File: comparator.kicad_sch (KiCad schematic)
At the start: 8 parts

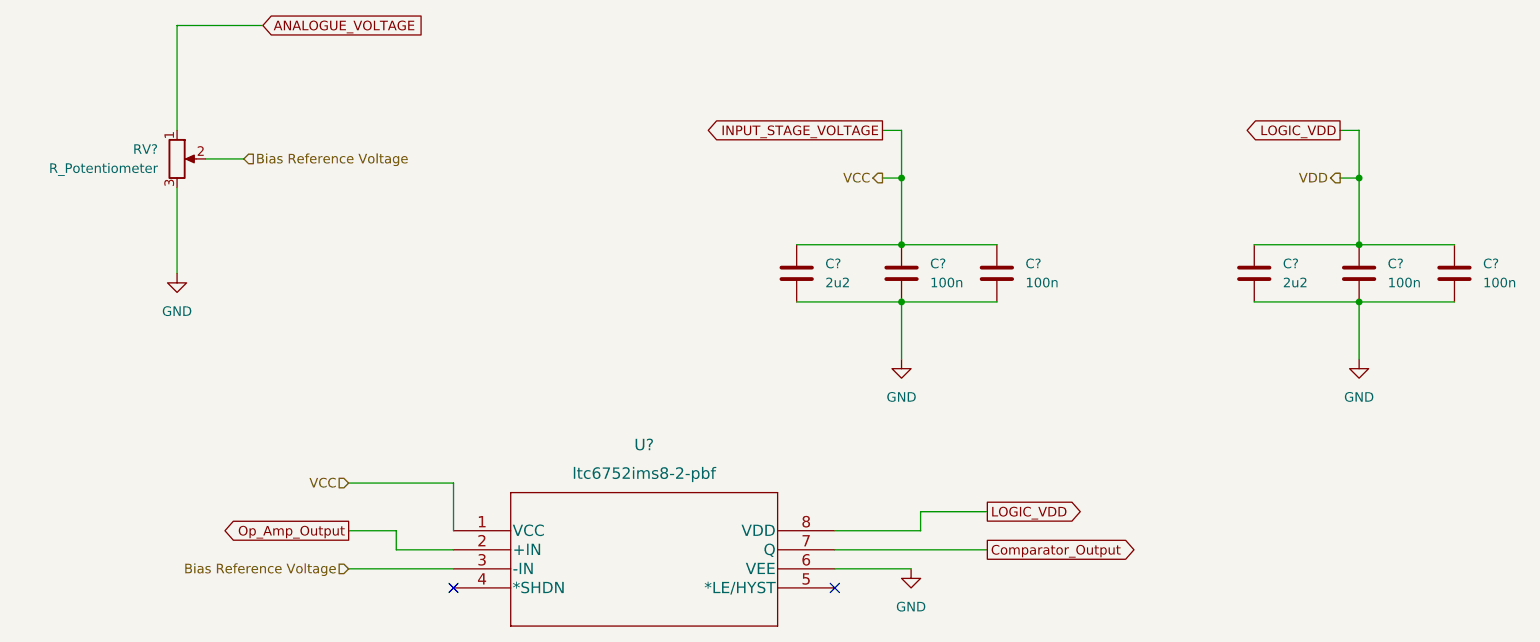
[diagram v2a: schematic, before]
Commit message: improve labels on comparator
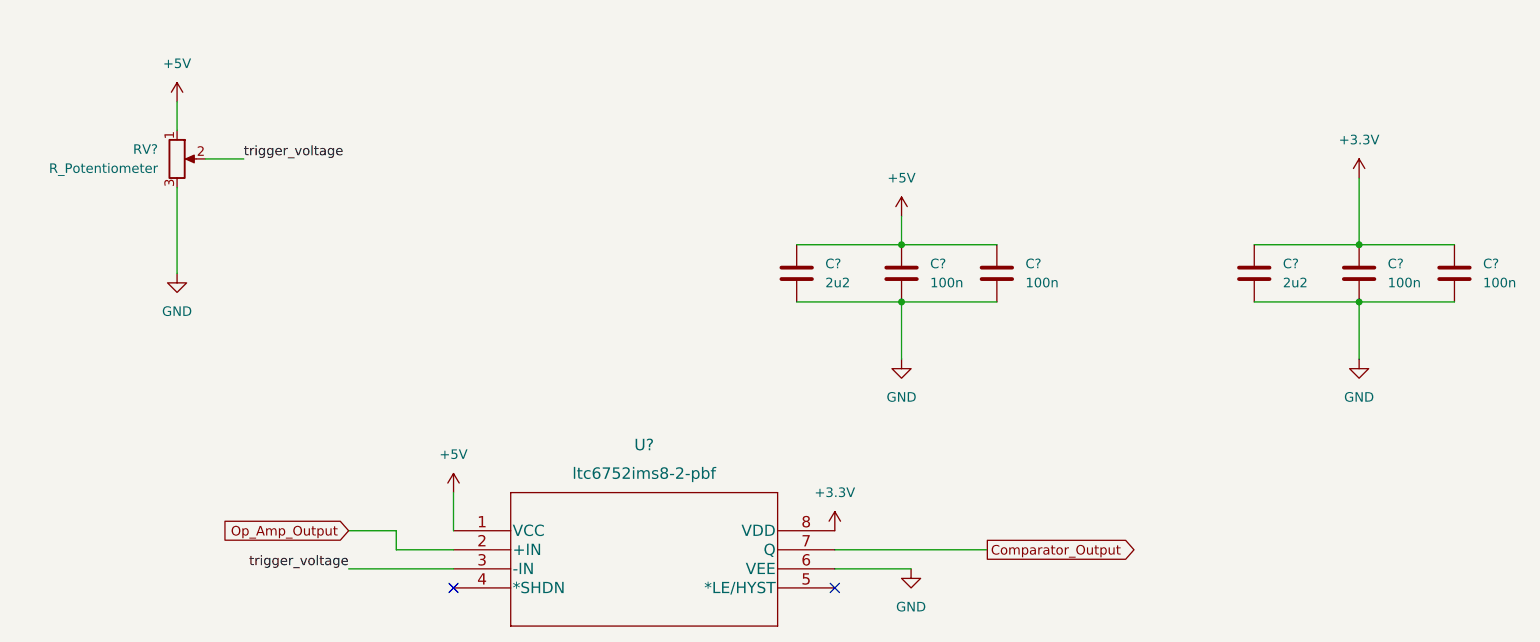
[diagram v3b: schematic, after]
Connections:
- net INPUT_STAGE_VOLTAGE is gone; now on net +5V: C?.1, C?.1, C?.1, U?.1 (VCC)
- net ANALOGUE_VOLTAGE renamed +5V
- net Bias Reference Voltage renamed trigger_voltage
- net LOGIC_VDD renamed +3.3V
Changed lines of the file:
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@@
   (junction (at 172.72 53.34) (diameter 0) (color 0 0 0 0)
   )
-  (junction (at 172.72 44.45) (diameter 0) (color 0 0 0 0)
-  )
   (junction (at 233.68 53.34) (diameter 0) (color 0 0 0 0)
   )
@@
   )
   (junction (at 172.72 60.96) (diameter 0) (color 0 0 0 0)
-  )
-  (junction (at 233.68 44.45) (diameter 0) (color 0 0 0 0)
   )
   (no_connect (at 113.03 99.06))
   (no_connect (at 163.83 99.06))
+  (wire (pts (xy 172.72 49.53) (xy 172.72 53.34))
+    (stroke (width 0) (type default) (color 0 0 0 0))
+  )
   (wire (pts (xy 233.68 60.96) (xy 246.38 60.96))
     (stroke (width 0) (type default) (color 0 0 0 0))
   )
-  (wire (pts (xy 172.72 44.45) (xy 172.72 53.34))
-    (stroke (width 0) (type default) (color 0 0 0 0))
-  )
-  (wire (pts (xy 170.18 38.1) (xy 172.72 38.1))
+  (wire (pts (xy 76.2 34.29) (xy 76.2 38.1))
+    (stroke (width 0) (type default) (color 0 0 0 0))
+  )
+  (wire (pts (xy 233.68 44.45) (xy 233.68 53.34))
     (stroke (width 0) (type default) (color 0 0 0 0))
   )
@@
     (stroke (width 0) (type default) (color 0 0 0 0))
   )
-  (wire (pts (xy 170.18 44.45) (xy 172.72 44.45))
-    (stroke (width 0) (type default) (color 0 0 0 0))
-  )
-  (wire (pts (xy 172.72 38.1) (xy 172.72 44.45))
-    (stroke (width 0) (type default) (color 0 0 0 0))
-  )
-  (wire (pts (xy 76.2 24.13) (xy 76.2 38.1))
-    (stroke (width 0) (type default) (color 0 0 0 0))
-  )
-  (wire (pts (xy 231.14 38.1) (xy 233.68 38.1))
-    (stroke (width 0) (type default) (color 0 0 0 0))
-  )
   (wire (pts (xy 163.83 96.52) (xy 173.99 96.52))
     (stroke (width 0) (type default) (color 0 0 0 0))
   )
-  (wire (pts (xy 175.26 88.9) (xy 184.15 88.9))
-    (stroke (width 0) (type default) (color 0 0 0 0))
-  )
   (wire (pts (xy 105.41 91.44) (xy 99.06 91.44))
     (stroke (width 0) (type default) (color 0 0 0 0))
   )
-  (wire (pts (xy 87.63 24.13) (xy 76.2 24.13))
-    (stroke (width 0) (type default) (color 0 0 0 0))
-  )
   (wire (pts (xy 158.75 53.34) (xy 172.72 53.34))
     (stroke (width 0) (type default) (color 0 0 0 0))
@@
     (stroke (width 0) (type default) (color 0 0 0 0))
   )
-  (wire (pts (xy 233.68 38.1) (xy 233.68 44.45))
+  (wire (pts (xy 172.72 53.34) (xy 185.42 53.34))
+    (stroke (width 0) (type default) (color 0 0 0 0))
+  )
+  (wire (pts (xy 113.03 86.36) (xy 113.03 91.44))
     (stroke (width 0) (type default) (color 0 0 0 0))
   )
@@
     (stroke (width 0) (type default) (color 0 0 0 0))
   )
-  (wire (pts (xy 163.83 91.44) (xy 175.26 91.44))
-    (stroke (width 0) (type default) (color 0 0 0 0))
-  )
   (wire (pts (xy 163.83 93.98) (xy 184.15 93.98))
     (stroke (width 0) (type default) (color 0 0 0 0))
   )
-  (wire (pts (xy 175.26 91.44) (xy 175.26 88.9))
-    (stroke (width 0) (type default) (color 0 0 0 0))
-  )
-  (wire (pts (xy 99.06 85.09) (xy 113.03 85.09))
-    (stroke (width 0) (type default) (color 0 0 0 0))
-  )
-  (wire (pts (xy 172.72 53.34) (xy 185.42 53.34))
-    (stroke (width 0) (type default) (color 0 0 0 0))
-  )
-  (wire (pts (xy 233.68 44.45) (xy 233.68 53.34))
-    (stroke (width 0) (type default) (color 0 0 0 0))
-  )
   (wire (pts (xy 105.41 93.98) (xy 105.41 91.44))
     (stroke (width 0) (type default) (color 0 0 0 0))
   )
-  (wire (pts (xy 113.03 91.44) (xy 113.03 85.09))
-    (stroke (width 0) (type default) (color 0 0 0 0))
-  )
   (wire (pts (xy 172.72 60.96) (xy 185.42 60.96))
     (stroke (width 0) (type default) (color 0 0 0 0))
@@
     (stroke (width 0) (type default) (color 0 0 0 0))
   )
-  (wire (pts (xy 231.14 44.45) (xy 233.68 44.45))
-    (stroke (width 0) (type default) (color 0 0 0 0))
-  )
   (wire (pts (xy 233.68 53.34) (xy 246.38 53.34))
     (stroke (width 0) (type default) (color 0 0 0 0))
@@
     (stroke (width 0) (type default) (color 0 0 0 0))
   )
-  (global_label "Op_Amp_Output" (shape output) (at 99.06 91.44 180) (fields_autoplaced)
+  (label "trigger_voltage" (at 99.06 96.52 180)
+    (effects (font (size 1.27 1.27)) (justify right bottom))
+  )
+  (label "trigger_voltage" (at 85.09 41.91 0)
+    (effects (font (size 1.27 1.27)) (justify left bottom))
+  )
+  (global_label "Op_Amp_Output" (shape input) (at 99.06 91.44 180) (fields_autoplaced)
     (effects (font (size 1.27 1.27)) (justify right))
     (property "Intersheet References" "${INTERSHEET_REFS}" (id 0) (at 82.0721 91.3606 0)
       (effects (font (size 1.27 1.27)) (justify right) hide)
-    )
-  )
-  (global_label "INPUT_STAGE_VOLTAGE" (shape output) (at 170.18 38.1 180) (fields_autoplaced)
-    (effects (font (size 1.27 1.27)) (justify right))
-    (property "Intersheet References" "${INTERSHEET_REFS}" (id 0) (at 146.7212 38.0206 0)
-      (effects (font (size 1.27 1.27)) (justify right) hide)
-    )
-  )
-  (global_label "LOGIC_VDD" (shape output) (at 184.15 88.9 0) (fields_autoplaced)
-    (effects (font (size 1.27 1.27)) (justify left))
-    (property "Intersheet References" "${INTERSHEET_REFS}" (id 0) (at 196.6626 88.8206 0)
-      (effects (font (size 1.27 1.27)) (justify left) hide)
     )
   )
@@
     )
   )
-  (global_label "ANALOGUE_VOLTAGE" (shape input) (at 87.63 24.13 0) (fields_autoplaced)
-    (effects (font (size 1.27 1.27)) (justify left))
-    (property "Intersheet References" "${INTERSHEET_REFS}" (id 0) (at 108.5488 24.0506 0)
-      (effects (font (size 1.27 1.27)) (justify left) hide)
-    )
-  )
-  (global_label "LOGIC_VDD" (shape output) (at 231.14 38.1 180) (fields_autoplaced)
-    (effects (font (size 1.27 1.27)) (justify right))
-    (property "Intersheet References" "${INTERSHEET_REFS}" (id 0) (at 218.6274 38.0206 0)
-      (effects (font (size 1.27 1.27)) (justify right) hide)
-    )
-  )
-  (hierarchical_label "Bias Reference Voltage" (shape input) (at 99.06 96.52 180)
-    (effects (font (size 1.27 1.27)) (justify right))
-  )
-  (hierarchical_label "VCC" (shape input) (at 99.06 85.09 180)
-    (effects (font (size 1.27 1.27)) (justify right))
-  )
-  (hierarchical_label "Bias Reference Voltage" (shape input) (at 85.09 41.91 0)
-    (effects (font (size 1.27 1.27)) (justify left))
-  )
-  (hierarchical_label "VDD" (shape output) (at 231.14 44.45 180)
-    (effects (font (size 1.27 1.27)) (justify right))
-  )
-  (hierarchical_label "VCC" (shape output) (at 170.18 44.45 180)
-    (effects (font (size 1.27 1.27)) (justify right))
-  )
   (symbol (lib_id "power:GND") (at 76.2 57.15 0) (unit 1)
     (in_bom yes) (on_board yes) (fields_autoplaced)
@@
     )
     (property "Datasheet" "" (id 3) (at 172.72 68.58 0)
+      (effects (font (size 1.27 1.27)) hide)
+    )
+    (pin "1")
+  )
+  (symbol (lib_id "power:+3.3V") (at 233.68 44.45 0) (unit 1)
+    (in_bom yes) (on_board yes) (fields_autoplaced)
+    (property "Reference" "#PWR?" (id 0) (at 233.68 48.26 0)
+      (effects (font (size 1.27 1.27)) hide)
+    )
+    (property "Value" "+3.3V" (id 1) (at 233.68 39.37 0))
+    (property "Footprint" "" (id 2) (at 233.68 44.45 0)
+      (effects (font (size 1.27 1.27)) hide)
+    )
+    (property "Datasheet" "" (id 3) (at 233.68 44.45 0)
       (effects (font (size 1.27 1.27)) hide)
     )
@@
     (pin "2")
   )
+  (symbol (lib_id "power:+5V") (at 113.03 86.36 0) (unit 1)
+    (in_bom yes) (on_board yes) (fields_autoplaced)
+    (property "Reference" "#PWR?" (id 0) (at 113.03 90.17 0)
+      (effects (font (size 1.27 1.27)) hide)
+    )
+    (property "Value" "+5V" (id 1) (at 113.03 81.28 0))
+    (property "Footprint" "" (id 2) (at 113.03 86.36 0)
+      (effects (font (size 1.27 1.27)) hide)
+    )
+    (property "Datasheet" "" (id 3) (at 113.03 86.36 0)
+      (effects (font (size 1.27 1.27)) hide)
+    )
+    (pin "1")
+  )
   (symbol (lib_id "Device:C") (at 246.38 57.15 0) (unit 1)
     (in_bom yes) (on_board yes) (fields_autoplaced)
@@
     (pin "1")
     (pin "2")
+  )
+  (symbol (lib_id "power:+3.3V") (at 163.83 91.44 0) (unit 1)
+    (in_bom yes) (on_board yes) (fields_autoplaced)
+    (property "Reference" "#PWR?" (id 0) (at 163.83 95.25 0)
+      (effects (font (size 1.27 1.27)) hide)
+    )
+    (property "Value" "+3.3V" (id 1) (at 163.83 86.36 0))
+    (property "Footprint" "" (id 2) (at 163.83 91.44 0)
+      (effects (font (size 1.27 1.27)) hide)
+    )
+    (property "Datasheet" "" (id 3) (at 163.83 91.44 0)
+      (effects (font (size 1.27 1.27)) hide)
+    )
+    (pin "1")
   )
   (symbol (lib_id "power:GND") (at 233.68 68.58 0) (unit 1)
@@
     (pin "2")
   )
+  (symbol (lib_id "power:+5V") (at 76.2 34.29 0) (unit 1)
+    (in_bom yes) (on_board yes) (fields_autoplaced)
+    (property "Reference" "#PWR?" (id 0) (at 76.2 38.1 0)
+      (effects (font (size 1.27 1.27)) hide)
+    )
+    (property "Value" "+5V" (id 1) (at 76.2 29.21 0))
+    (property "Footprint" "" (id 2) (at 76.2 34.29 0)
+      (effects (font (size 1.27 1.27)) hide)
+    )
+    (property "Datasheet" "" (id 3) (at 76.2 34.29 0)
+      (effects (font (size 1.27 1.27)) hide)
+    )
+    (pin "1")
+  )
   (symbol (lib_id "Device:C") (at 219.71 57.15 0) (unit 1)
     (in_bom yes) (on_board yes) (fields_autoplaced)
@@
     (pin "2")
   )
+  (symbol (lib_id "power:+5V") (at 172.72 49.53 0) (unit 1)
+    (in_bom yes) (on_board yes) (fields_autoplaced)
+    (property "Reference" "#PWR?" (id 0) (at 172.72 53.34 0)
+      (effects (font (size 1.27 1.27)) hide)
+    )
+    (property "Value" "+5V" (id 1) (at 172.72 44.45 0))
+    (property "Footprint" "" (id 2) (at 172.72 49.53 0)
+      (effects (font (size 1.27 1.27)) hide)
+    )
+    (property "Datasheet" "" (id 3) (at 172.72 49.53 0)
+      (effects (font (size 1.27 1.27)) hide)
+    )
+    (pin "1")
+  )
 )

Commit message: add component numbers to schematic
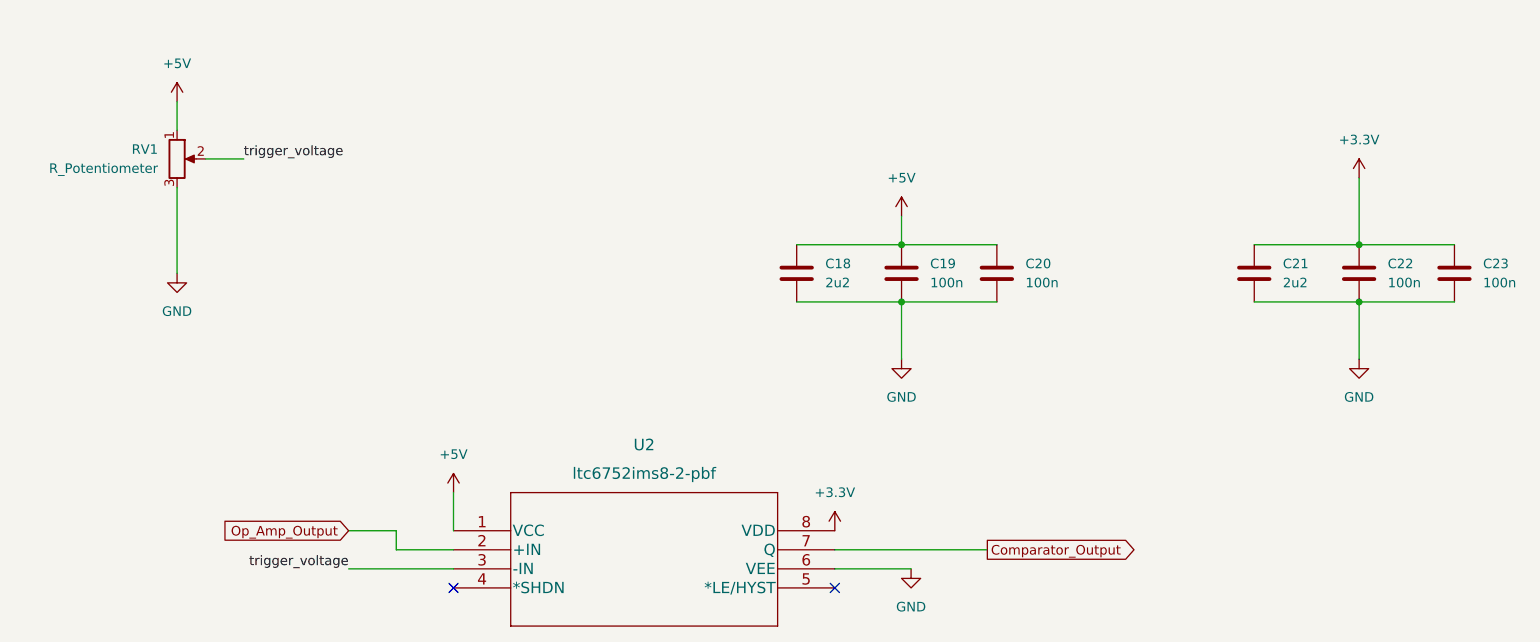
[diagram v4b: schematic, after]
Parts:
- gave numbers to parts that had none: 8
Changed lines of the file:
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@@
   (symbol (lib_id "power:GND") (at 76.2 57.15 0) (unit 1)
     (in_bom yes) (on_board yes) (fields_autoplaced)
-    (property "Reference" "#PWR?" (id 0) (at 76.2 63.5 0)
+    (property "Reference" "#PWR030" (id 0) (at 76.2 63.5 0)
       (effects (font (size 1.27 1.27)) hide)
     )
@@
   (symbol (lib_id "power:GND") (at 173.99 96.52 0) (unit 1)
     (in_bom yes) (on_board yes) (fields_autoplaced)
-    (property "Reference" "#PWR?" (id 0) (at 173.99 102.87 0)
+    (property "Reference" "#PWR035" (id 0) (at 173.99 102.87 0)
       (effects (font (size 1.27 1.27)) hide)
     )
@@
   (symbol (lib_id "power:GND") (at 172.72 68.58 0) (unit 1)
     (in_bom yes) (on_board yes) (fields_autoplaced)
-    (property "Reference" "#PWR?" (id 0) (at 172.72 74.93 0)
+    (property "Reference" "#PWR034" (id 0) (at 172.72 74.93 0)
       (effects (font (size 1.27 1.27)) hide)
     )
@@
   (symbol (lib_id "power:+3.3V") (at 233.68 44.45 0) (unit 1)
     (in_bom yes) (on_board yes) (fields_autoplaced)
-    (property "Reference" "#PWR?" (id 0) (at 233.68 48.26 0)
+    (property "Reference" "#PWR036" (id 0) (at 233.68 48.26 0)
       (effects (font (size 1.27 1.27)) hide)
     )
@@
   (symbol (lib_id "Device:C") (at 158.75 57.15 0) (unit 1)
     (in_bom yes) (on_board yes) (fields_autoplaced)
-    (property "Reference" "C?" (id 0) (at 162.56 55.8799 0)
+    (property "Reference" "C18" (id 0) (at 162.56 55.8799 0)
       (effects (font (size 1.27 1.27)) (justify left))
     )
@@
   (symbol (lib_id "Comparator:ltc6752ims8-2-pbf") (at 113.03 91.44 0) (unit 1)
     (in_bom yes) (on_board yes) (fields_autoplaced)
-    (property "Reference" "U?" (id 0) (at 138.43 80.01 0)
+    (property "Reference" "U2" (id 0) (at 138.43 80.01 0)
       (effects (font (size 1.524 1.524)))
     )
@@
   (symbol (lib_id "Device:R_Potentiometer") (at 76.2 41.91 0) (unit 1)
     (in_bom yes) (on_board yes) (fields_autoplaced)
-    (property "Reference" "RV?" (id 0) (at 73.66 40.6399 0)
+    (property "Reference" "RV1" (id 0) (at 73.66 40.6399 0)
       (effects (font (size 1.27 1.27)) (justify right))
     )
@@
   (symbol (lib_id "Device:C") (at 172.72 57.15 0) (unit 1)
     (in_bom yes) (on_board yes) (fields_autoplaced)
-    (property "Reference" "C?" (id 0) (at 176.53 55.8799 0)
+    (property "Reference" "C19" (id 0) (at 176.53 55.8799 0)
       (effects (font (size 1.27 1.27)) (justify left))
     )
@@
   (symbol (lib_id "Device:C") (at 233.68 57.15 0) (unit 1)
     (in_bom yes) (on_board yes) (fields_autoplaced)
-    (property "Reference" "C?" (id 0) (at 237.49 55.8799 0)
+    (property "Reference" "C22" (id 0) (at 237.49 55.8799 0)
       (effects (font (size 1.27 1.27)) (justify left))
     )
@@
   (symbol (lib_id "power:+5V") (at 113.03 86.36 0) (unit 1)
     (in_bom yes) (on_board yes) (fields_autoplaced)
-    (property "Reference" "#PWR?" (id 0) (at 113.03 90.17 0)
+    (property "Reference" "#PWR031" (id 0) (at 113.03 90.17 0)
       (effects (font (size 1.27 1.27)) hide)
     )
@@
   (symbol (lib_id "Device:C") (at 246.38 57.15 0) (unit 1)
     (in_bom yes) (on_board yes) (fields_autoplaced)
-    (property "Reference" "C?" (id 0) (at 250.19 55.8799 0)
+    (property "Reference" "C23" (id 0) (at 250.19 55.8799 0)
       (effects (font (size 1.27 1.27)) (justify left))
     )
@@
   (symbol (lib_id "power:+3.3V") (at 163.83 91.44 0) (unit 1)
     (in_bom yes) (on_board yes) (fields_autoplaced)
-    (property "Reference" "#PWR?" (id 0) (at 163.83 95.25 0)
+    (property "Reference" "#PWR032" (id 0) (at 163.83 95.25 0)
       (effects (font (size 1.27 1.27)) hide)
     )
@@
   (symbol (lib_id "power:GND") (at 233.68 68.58 0) (unit 1)
     (in_bom yes) (on_board yes) (fields_autoplaced)
-    (property "Reference" "#PWR?" (id 0) (at 233.68 74.93 0)
+    (property "Reference" "#PWR037" (id 0) (at 233.68 74.93 0)
       (effects (font (size 1.27 1.27)) hide)
     )
@@
   (symbol (lib_id "Device:C") (at 185.42 57.15 0) (unit 1)
     (in_bom yes) (on_board yes) (fields_autoplaced)
-    (property "Reference" "C?" (id 0) (at 189.23 55.8799 0)
+    (property "Reference" "C20" (id 0) (at 189.23 55.8799 0)
       (effects (font (size 1.27 1.27)) (justify left))
     )
@@
   (symbol (lib_id "power:+5V") (at 76.2 34.29 0) (unit 1)
     (in_bom yes) (on_board yes) (fields_autoplaced)
-    (property "Reference" "#PWR?" (id 0) (at 76.2 38.1 0)
+    (property "Reference" "#PWR029" (id 0) (at 76.2 38.1 0)
       (effects (font (size 1.27 1.27)) hide)
     )
@@
   (symbol (lib_id "Device:C") (at 219.71 57.15 0) (unit 1)
     (in_bom yes) (on_board yes) (fields_autoplaced)
-    (property "Reference" "C?" (id 0) (at 223.52 55.8799 0)
+    (property "Reference" "C21" (id 0) (at 223.52 55.8799 0)
       (effects (font (size 1.27 1.27)) (justify left))
     )
@@
   (symbol (lib_id "power:+5V") (at 172.72 49.53 0) (unit 1)
     (in_bom yes) (on_board yes) (fields_autoplaced)
-    (property "Reference" "#PWR?" (id 0) (at 172.72 53.34 0)
-      (effects (font (size 1.27 1.27)) hide)
-    )
+    (property "Reference" "#PWR033" (id 0) (at 172.72 53.34 0)
+      (effects (font (size 1.27 1.27)) hide)
+    )

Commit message: Assign footprints to ICs
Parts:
- U2: footprint MSOP-8_MS -> Package_SO:MSOP-8_3x3mm_P0.65mm
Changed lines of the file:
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@@
       (effects (font (size 1.524 1.524)))
     )
-    (property "Footprint" "MSOP-8_MS" (id 2) (at 138.43 85.344 0)
+    (property "Footprint" "Package_SO:MSOP-8_3x3mm_P0.65mm" (id 2) (at 138.43 85.344 0)
       (effects (font (size 1.524 1.524)) hide)
     )
